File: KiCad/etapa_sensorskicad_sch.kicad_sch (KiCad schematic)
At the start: 20 parts, among them J5 Conn_01x04_Pin, K1 Fujitsu_FTR-LYAA005x, K2 Fujitsu_FTR-LYAA005x, U23 FXTH87, U6 FDC2214, U7 FXTH87

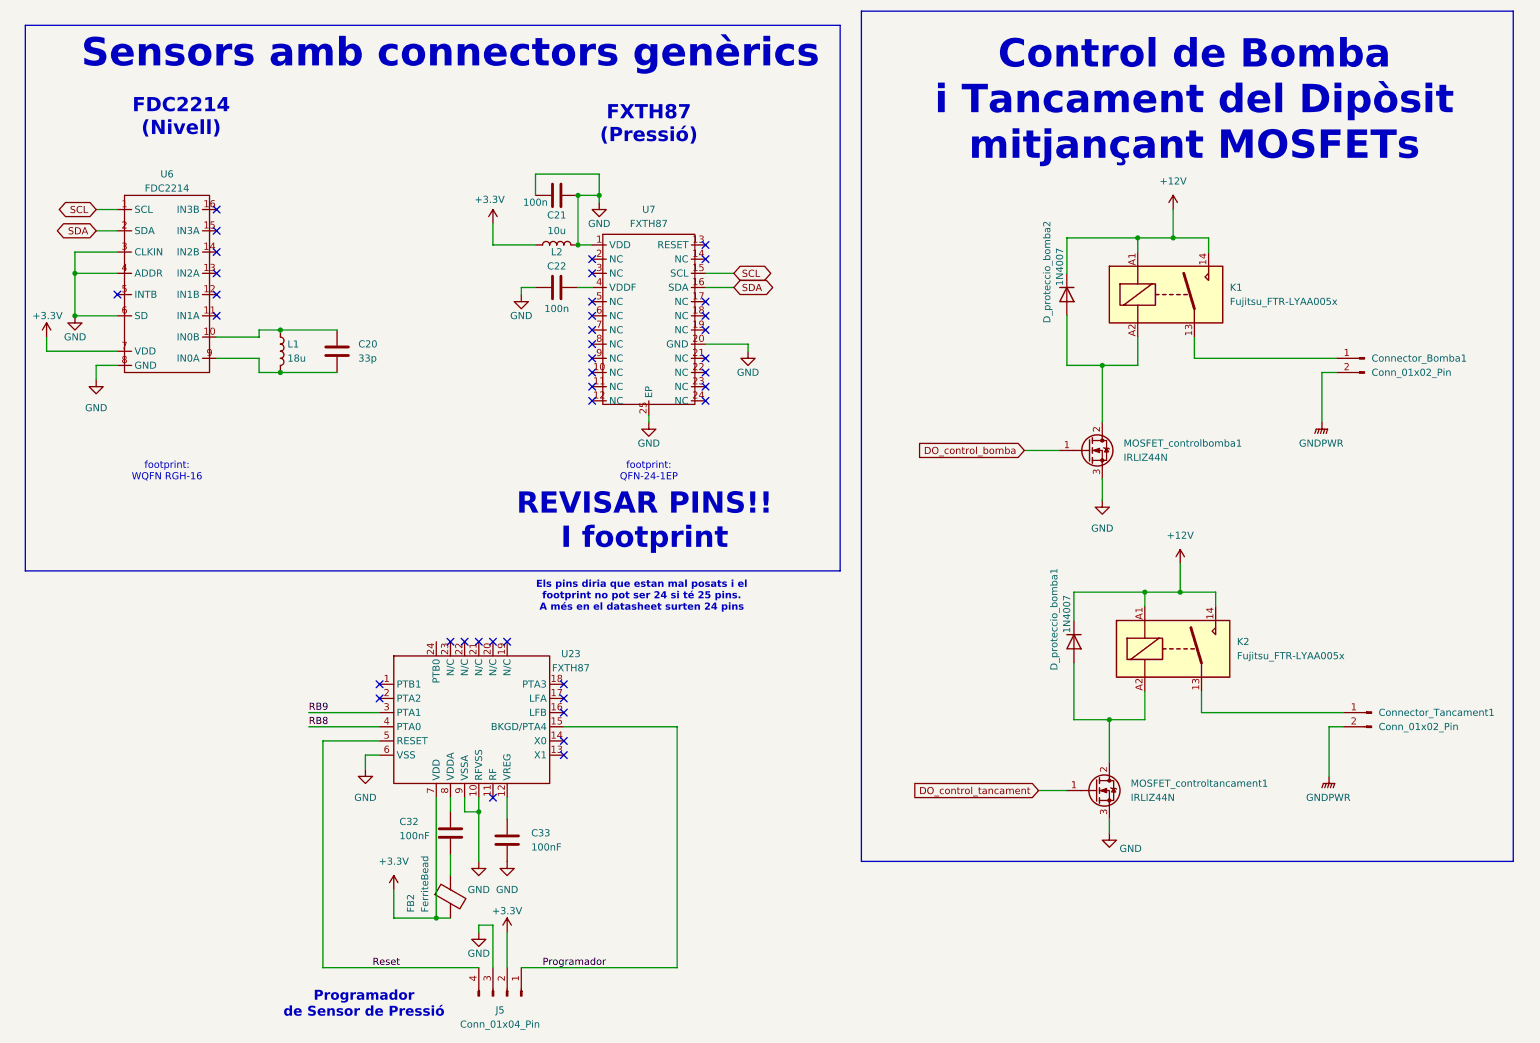
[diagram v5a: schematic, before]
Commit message: Posem una part que estava en el subesquemàtic de sesnors al de potència (el control de la bomba i del dipòsit)
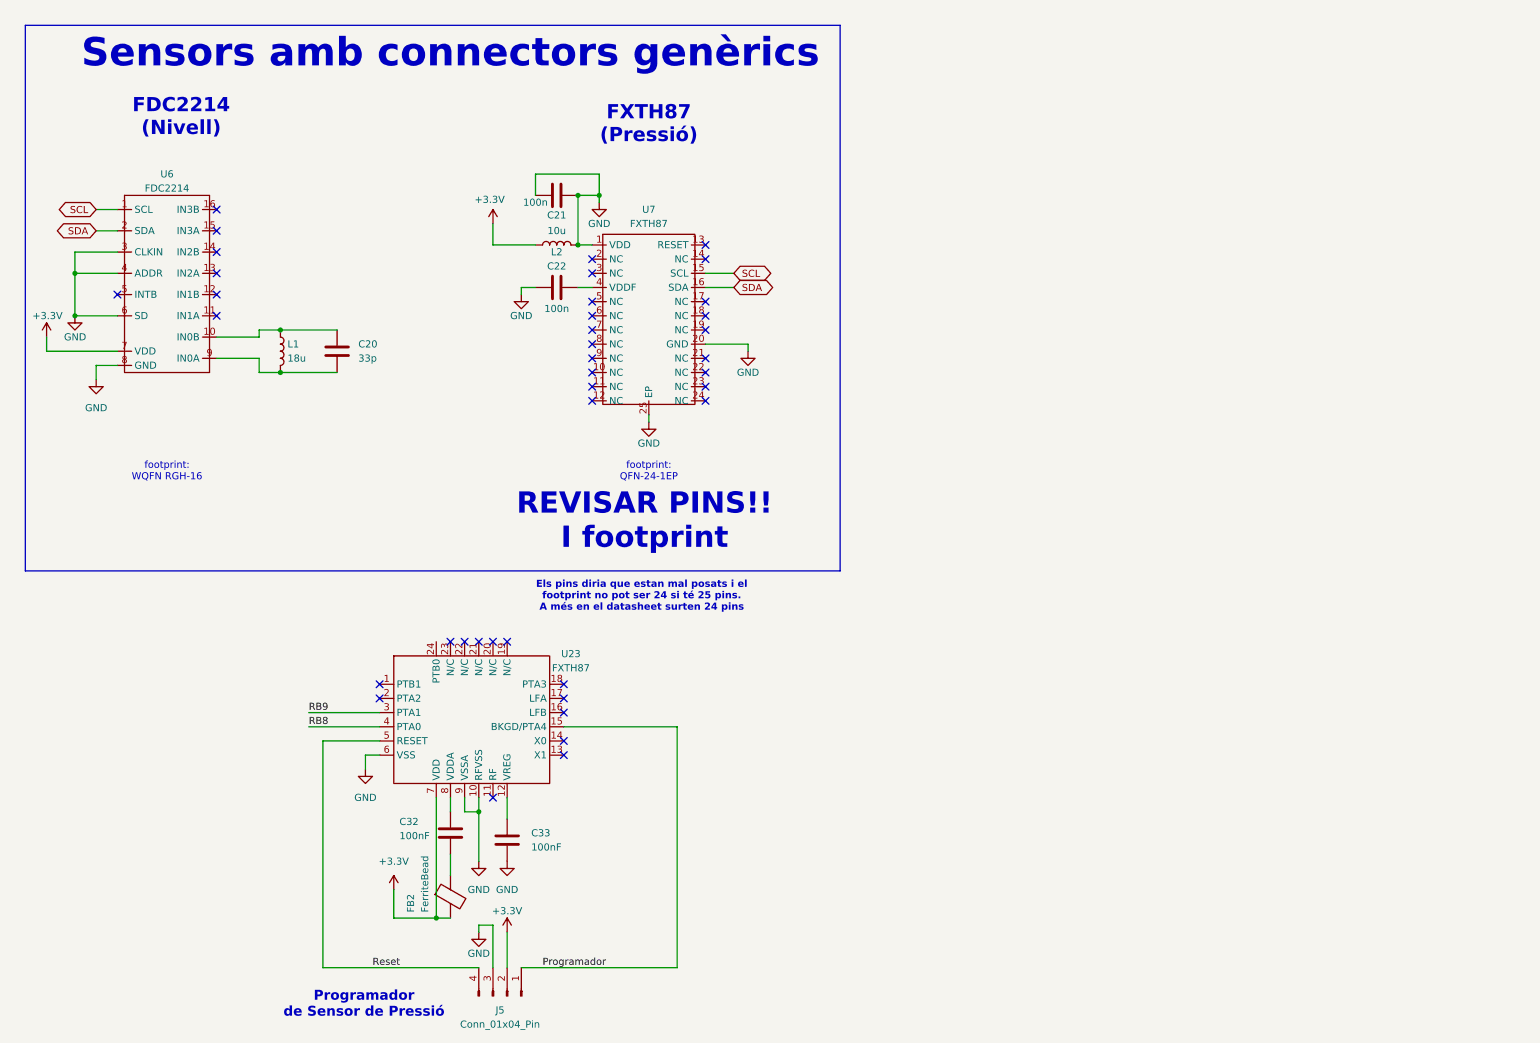
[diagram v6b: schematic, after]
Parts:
- removed Connector_Bomba1, Connector_Tancament1: Conn_01x02_Pin, Connector_PinHeader_2.54mm:PinHeader_1x02_P2.54mm_Vertical, symbol Connector:Conn_01x02_Pin
- removed D_proteccio_bomba1, D_proteccio_bomba2: 1N4007, symbol Device:D
- removed K1, K2: Fujitsu_FTR-LYAA005x, Relay_THT:Relay_SPST-NO_Fujitsu_FTR-LYAA005x_FormA_Vertical, symbol Relay:Fujitsu_FTR-LYAA005x
- removed MOSFET_controlbomba1, MOSFET_controltancament1: IRLIZ44N, Package_TO_SOT_THT:TO-220F-3_Vertical, symbol Transistor_FET:IRLIZ44N
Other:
- note removed: "Control de Bomba i Tancament del Dipòsit mitjançant MOSFETs"

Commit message: push ràpid, falta pull ups del sensor de pressio al micro
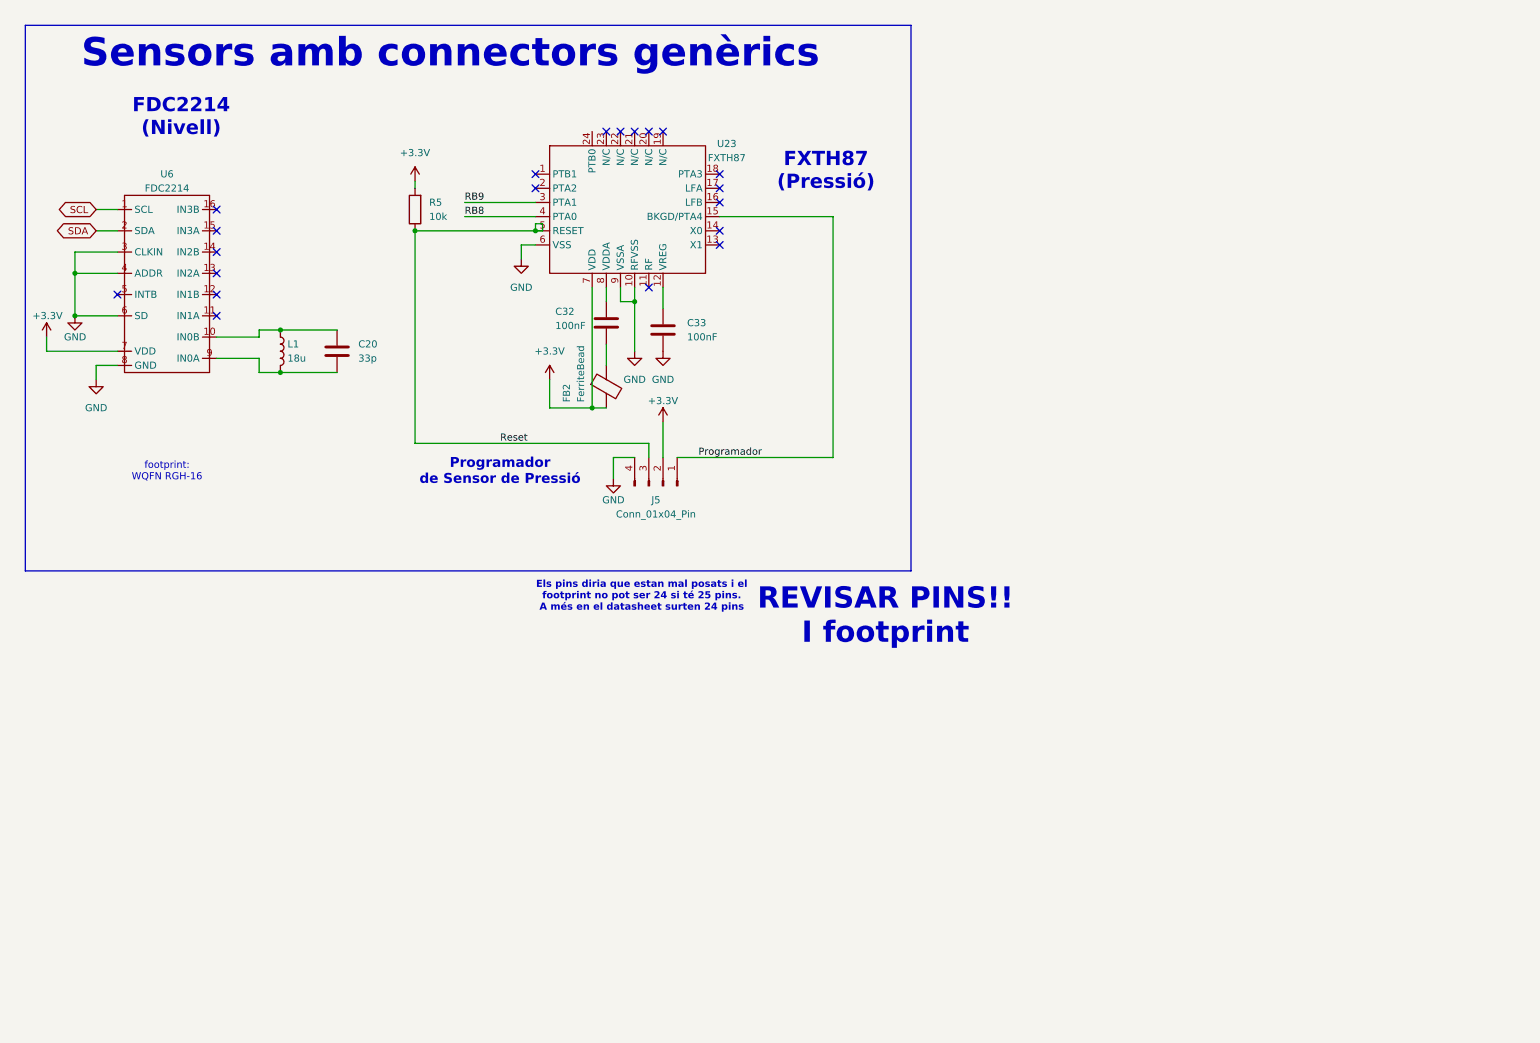
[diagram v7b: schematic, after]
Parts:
- removed C21, C22: 100n, symbol Device:C
- removed L2: 10u, symbol Device:L
- removed U7: FXTH87, symbol Sensors_Custom:FXTH87
- added R5: 10k, symbol Device:R
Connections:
- net +3.3V: now also R5.2
- net GND: now also J5.4 (Pin_4); no longer J5.3 (Pin_3)
- net Reset: now also J5.3 (Pin_3), R5.1; no longer J5.4 (Pin_4)
- no-connect marks 39 -> 20
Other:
- note removed: "footprint: QFN-24-1EP"
- moved on the sheet: C32, C33, FB2, J5, U23

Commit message: Esquemàtic ACABAT
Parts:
- C20, C32, C33: footprint (none) -> Capacitor_SMD:C_0805_2012Metric
- L1: footprint (none) -> Inductor_SMD:L_0805_2012Metric
- R5: footprint (none) -> Resistor_SMD:R_0805_2012Metric
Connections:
- net RB8 renamed CNTRL
- net RB9 renamed PWM
- no-connect marks 20 -> 21
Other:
- note added: "Programar sensor per rebre enviar senyals PWM"
- note removed: "Els pins diria que estan mal posats i el footprint no pot ser 24 si té 25 pins. A més en el datasheet surten 24 pins"
- note removed: "REVISAR PINS!! I footprint"
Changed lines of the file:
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@@
-		)
-	)
-	(text "Els pins diria que estan mal posats i el \nfootprint no pot ser 24 si té 25 pins.\nA més en el datasheet surten 24 pins"
-		(exclude_from_sim no)
-		(at 125.73 118.872 0)
-		(effects
-			(font
-				(size 1.27 1.27)
-				(thickness 0.254)
-				(bold yes)
-			)
 		)
 	)
@@
 	(text "Programador\nde Sensor de Pressió"
 		(exclude_from_sim no)
-		(at 100.33 96.52 0)
+		(at 128.27 109.474 0)
 		(effects
 			(font
@@
 		)
 	)
-	(text "REVISAR PINS!!\nI footprint"
-		(exclude_from_sim no)
-		(at 169.418 122.428 0)
+	(text "Programar sensor \nper rebre enviar \nsenyals PWM"
+		(exclude_from_sim no)
+		(at 98.806 39.37 0)
 		(effects
 			(font
-				(size 3.81 3.81)
-				(thickness 1.016)
-				(bold yes)
+				(size 1.27 1.27)
 			)
 		)
@@
 	)
 	(junction
-		(at 60.96 78.74)
+		(at 85.09 53.34)
 		(diameter 0)
 		(color 0 0 0 0)
 	)
 	(junction
-		(at 85.09 53.34)
+		(at 60.96 78.74)
 		(diameter 0)
 		(color 0 0 0 0)
@@
 		(color 0 0 0 0)
 	)
-	(junction
-		(at 106.68 53.34)
-		(diameter 0)
-		(color 0 0 0 0)
-	)
 	(no_connect
 		(at 139.7 45.72)
@@
 	)
 	(no_connect
+		(at 116.84 35.56)
+	)
+	(no_connect
 		(at 139.7 48.26)
 	)
@@
 	(wire
 		(pts
-			(xy 106.68 52.07) (xy 106.68 53.34)
-		)
-		(stroke
-			(width 0)
-			(type default)
-		)
-	)
-	(wire
-		(pts
 			(xy 127 91.44) (xy 85.09 91.44)
 		)
@@
 	(wire
 		(pts
+			(xy 95.25 50.8) (xy 106.68 50.8)
+		)
+		(stroke
+			(width 0)
+			(type default)
+		)
+	)
+	(wire
+		(pts
 			(xy 121.92 66.04) (xy 124.46 66.04)
 		)
@@
 	(wire
 		(pts
-			(xy 93.98 50.8) (xy 106.68 50.8)
-		)
-		(stroke
-			(width 0)
-			(type default)
-		)
-	)
-	(wire
-		(pts
-			(xy 106.68 53.34) (xy 107.95 53.34)
-		)
-		(stroke
-			(width 0)
-			(type default)
-		)
-	)
-	(wire
-		(pts
-			(xy 107.95 52.07) (xy 106.68 52.07)
-		)
-		(stroke
-			(width 0)
-			(type default)
-		)
-	)
-	(wire
-		(pts
 			(xy 160.02 50.8) (xy 139.7 50.8)
 		)
@@
 	(wire
 		(pts
-			(xy 107.95 53.34) (xy 107.95 52.07)
-		)
-		(stroke
-			(width 0)
-			(type default)
-		)
-	)
-	(wire
-		(pts
 			(xy 31.75 57.15) (xy 24.13 57.15)
 		)
@@
 	(wire
 		(pts
+			(xy 124.46 93.98) (xy 120.65 93.98)
+		)
+		(stroke
+			(width 0)
+			(type default)
+		)
+	)
+	(wire
+		(pts
+			(xy 24.13 57.15) (xy 24.13 60.96)
+		)
+		(stroke
+			(width 0)
+			(type default)
+		)
+	)
+	(wire
+		(pts
+			(xy 49.53 72.39) (xy 57.15 72.39)
+		)
+		(stroke
+			(width 0)
+			(type default)
+		)
+	)
+	(wire
+		(pts
+			(xy 24.13 60.96) (xy 31.75 60.96)
+		)
+		(stroke
+			(width 0)
+			(type default)
+		)
+	)
+	(bus
+		(pts
+			(xy 15.24 16.51) (xy 15.24 114.3)
+		)
+		(stroke
+			(width 0)
+			(type default)
+		)
+	)
+	(bus
+		(pts
+			(xy 173.99 114.3) (xy 15.24 114.3)
+		)
+		(stroke
+			(width 0)
+			(type default)
+		)
+	)
+	(wire
+		(pts
+			(xy 57.15 78.74) (xy 60.96 78.74)
+		)
+		(stroke
+			(width 0)
+			(type default)
+		)
+	)
+	(wire
+		(pts
 			(xy 93.98 48.26) (xy 106.68 48.26)
 		)
@@
 	(wire
 		(pts
-			(xy 124.46 93.98) (xy 120.65 93.98)
-		)
-		(stroke
-			(width 0)
-			(type default)
-		)
-	)
-	(wire
-		(pts
-			(xy 24.13 57.15) (xy 24.13 60.96)
-		)
-		(stroke
-			(width 0)
-			(type default)
-		)
-	)
-	(wire
-		(pts
-			(xy 49.53 72.39) (xy 57.15 72.39)
-		)
-		(stroke
-			(width 0)
-			(type default)
-		)
-	)
-	(wire
-		(pts
-			(xy 24.13 60.96) (xy 31.75 60.96)
-		)
-		(stroke
-			(width 0)
-			(type default)
-		)
-	)
-	(bus
-		(pts
-			(xy 15.24 16.51) (xy 15.24 114.3)
-		)
-		(stroke
-			(width 0)
-			(type default)
-		)
-	)
-	(bus
-		(pts
-			(xy 173.99 114.3) (xy 15.24 114.3)
-		)
-		(stroke
-			(width 0)
-			(type default)
-		)
-	)
-	(wire
-		(pts
-			(xy 57.15 78.74) (xy 60.96 78.74)
+			(xy 85.09 53.34) (xy 106.68 53.34)
 		)
 		(stroke
@@
 	(wire
 		(pts
-			(xy 85.09 53.34) (xy 106.68 53.34)
-		)
-		(stroke
-			(width 0)
-			(type default)
-		)
-	)
-	(wire
-		(pts
 			(xy 27.94 77.47) (xy 27.94 80.01)
 		)
@@
 			(width 0)
 			(type default)
-		)
-	)
-	(label "RB8"
-		(at 93.98 50.8 0)
-		(effects
-			(font
-				(size 1.27 1.27)
-			)
-			(justify left bottom)
-		)
-	)
-	(label "RB9"
-		(at 93.98 48.26 0)
-		(effects
-			(font
-				(size 1.27 1.27)
-			)
-			(justify left bottom)
 		)
 	)
@@
 		)
 	)
+	(global_label "PWM"
+		(shape input)
+		(at 93.98 48.26 180)
+		(fields_autoplaced yes)
+		(effects
+			(font
+				(size 1.27 1.27)
+			)
+			(justify right)
+		)
+		(property "Intersheetrefs" "${INTERSHEET_REFS}"
+			(at 86.822 48.26 0)
+			(effects
+				(font
+					(size 1.27 1.27)
+				)
+				(justify right)
+				(hide yes)
+			)
+		)
+	)
+	(global_label "CNTRL"
+		(shape input)
+		(at 95.25 50.8 180)
+		(fields_autoplaced yes)
+		(effects
+			(font
+				(size 1.27 1.27)
+			)
+			(justify right)
+		)
+		(property "Intersheetrefs" "${INTERSHEET_REFS}"
+			(at 86.3986 50.8 0)
+			(effects
+				(font
+					(size 1.27 1.27)
+				)
+				(justify right)
+				(hide yes)
+			)
+		)
+	)
 	(global_label "SDA"
 		(shape bidirectional)
@@
 			)
 		)
-		(property "Footprint" ""
+		(property "Footprint" "Capacitor_SMD:C_0805_2012Metric"
 			(at 130.5052 74.93 0)
 			(effects
@@
 		(on_board yes)
 		(dnp no)
-		(fields_autoplaced yes)
 		(property "Reference" "J5"
 			(at 128.27 101.6 90)
@@
 			)
 		)
-		(property "Footprint" ""
+		(property "Footprint" "Capacitor_SMD:C_0805_2012Metric"
 			(at 72.0852 78.74 0)
 			(effects
@@
 		(fields_autoplaced yes)
 		(property "Reference" "U23"
-			(at 140.97 37.7346 0)
+			(at 142.24 36.7598 0)
 			(effects
 				(font
@@
 		)
 		(property "Value" "FXTH87"
-			(at 140.97 40.2746 0)
+			(at 142.24 39.2998 0)
 			(effects
 				(font
@@
 			)
 		)
-		(property "Footprint" ""
+		(property "Footprint" "Inductor_SMD:L_0805_2012Metric"
 			(at 60.96 74.93 0)
 			(effects
@@
 		(on_board yes)
 		(dnp no)
-		(fields_autoplaced yes)
 		(property "Reference" "R5"
-			(at 87.63 48.2599 0)
+			(at 80.264 48.26 0)
 			(effects
 				(font
@@
 		)
 		(property "Value" "10k"
-			(at 87.63 50.7999 0)
+			(at 79.756 50.8 0)
 			(effects
 				(font
@@
 			)
 		)
-		(property "Footprint" ""
+		(property "Footprint" "Resistor_SMD:R_0805_2012Metric"
 			(at 86.868 49.53 90)
 			(effects
@@
 			)
 		)
-		(property "Footprint" ""
+		(property "Footprint" "Capacitor_SMD:C_0805_2012Metric"
 			(at 120.3452 73.66 0)
 			(effects
